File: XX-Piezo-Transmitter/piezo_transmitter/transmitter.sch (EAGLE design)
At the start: 6 parts, among them U1 BD6221FSOP, U2 ATTINY24A-SSUR

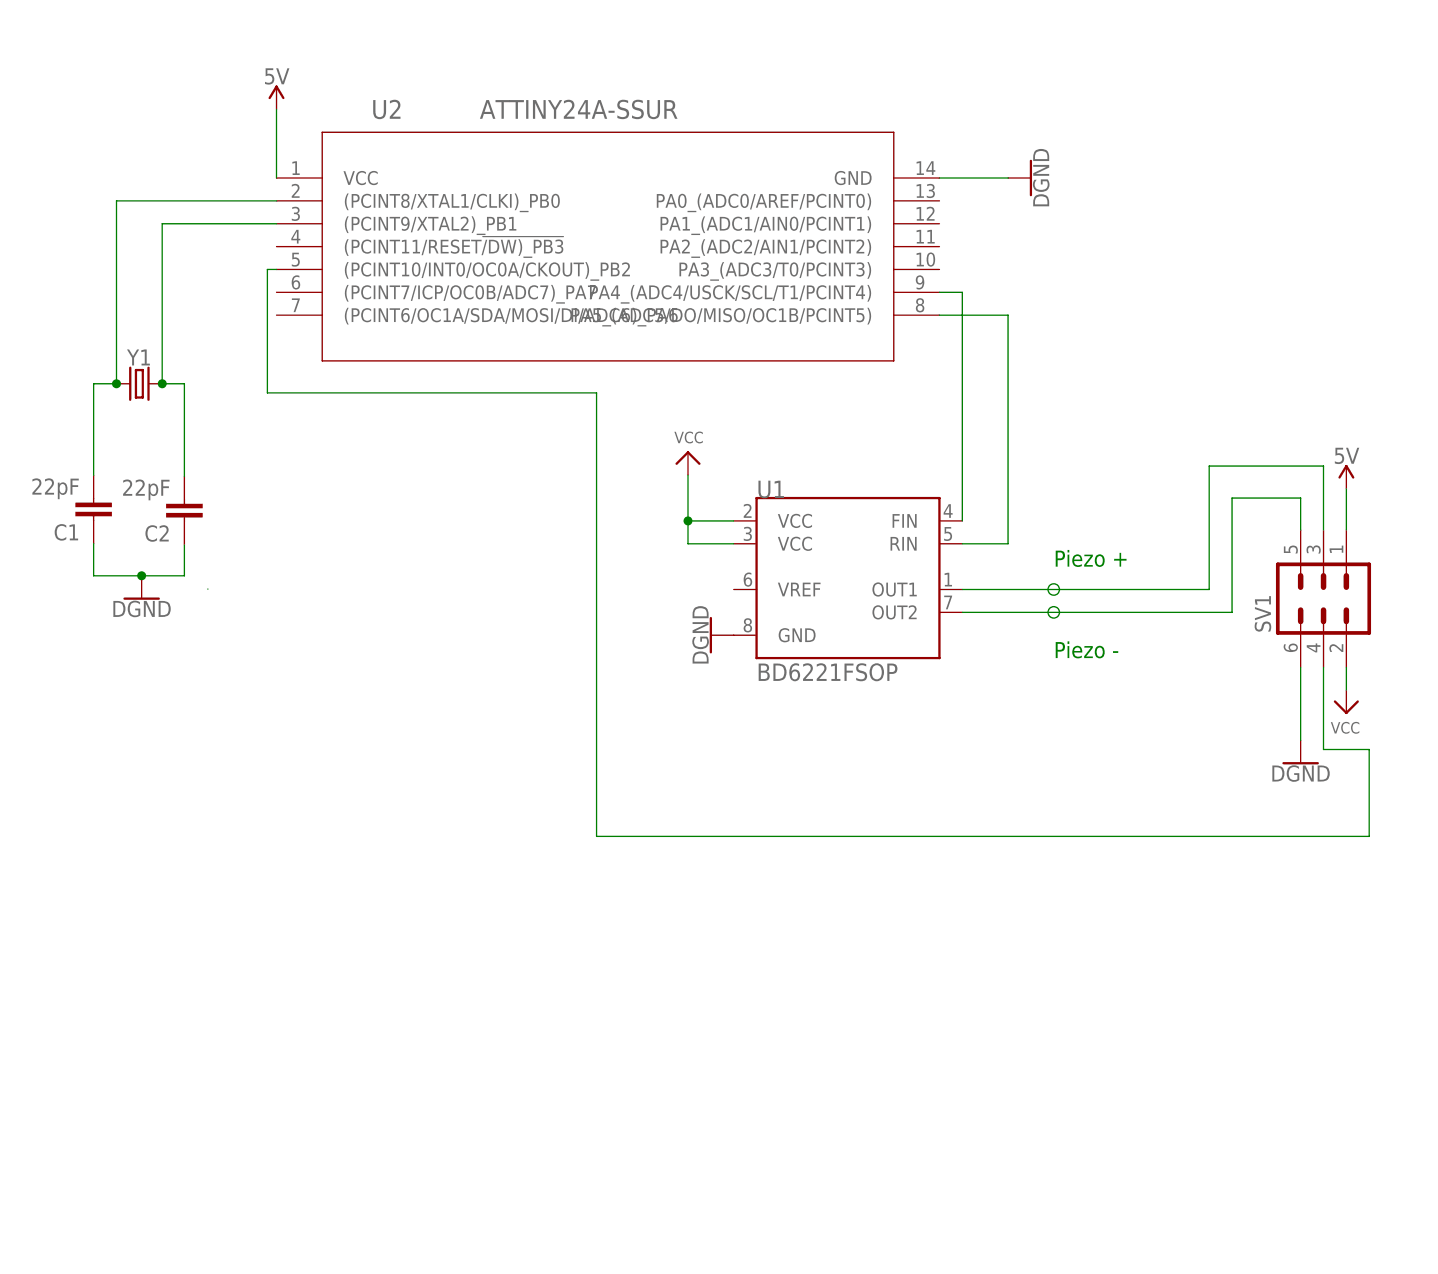
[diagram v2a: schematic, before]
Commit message: Fixed oscillator trace lengths and board trace widths. Added programmer header and mounting holes. Board about 1 squ in now.
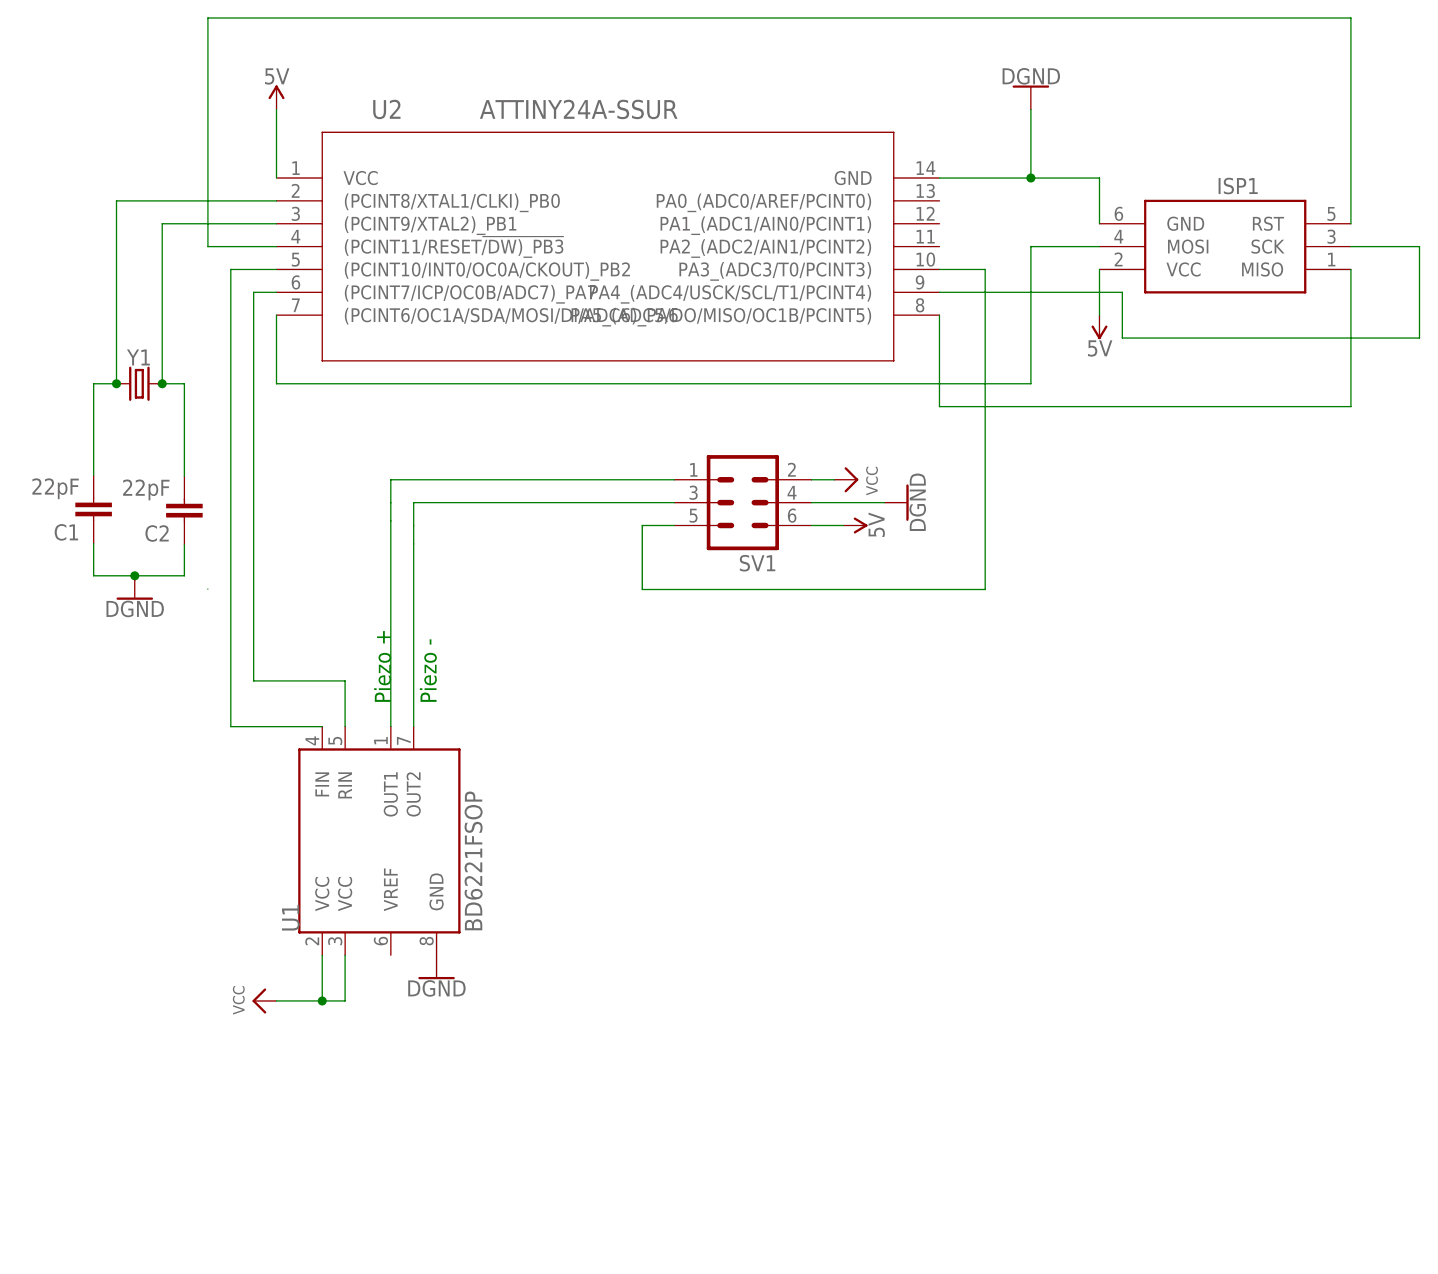
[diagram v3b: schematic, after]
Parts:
- added ISP1: AVRISP-6, adafruit:AVRISP-6
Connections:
- removed net FIN: U1.FIN, U2.PA4_(ADC4/USCK/SCL/T1/PCINT4)
- removed net PIEZO+: SV1.3, U1.OUT1
- removed net PIEZO-: SV1.5, U1.OUT2
- removed net PWM: SV1.4, U2.(PCINT10/INT0/OC0A/CKOUT)_PB2
- removed net RIN: U1.RIN, U2.PA5_(ADC5/DO/MISO/OC1B/PCINT5)
- new net N$10: U1.RIN, U2.(PCINT7/ICP/OC0B/ADC7)_PA7
- new net N$11: ISP1.SCK, U2.PA4_(ADC4/USCK/SCL/T1/PCINT4)
- new net N$12: ISP1.MISO, U2.PA5_(ADC5/DO/MISO/OC1B/PCINT5)
- new net N$4: ISP1.MOSI, U2.(PCINT6/OC1A/SDA/MOSI/DI/ADC6)_PA6
- new net N$5: SV1.5, U2.PA3_(ADC3/T0/PCINT3)
- new net N$6: ISP1.RST, U2.(PCINT11/RESET!/DW)_PB3
- new net N$7: SV1.1, U1.OUT1
- new net N$8: SV1.3, U1.OUT2
- new net N$9: U1.FIN, U2.(PCINT10/INT0/OC0A/CKOUT)_PB2
- net GND: now also ISP1.GND, SV1.4; no longer SV1.6
- net VCC_2: now also ISP1.VCC, SV1.6; no longer SV1.1
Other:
- moved on the sheet: SV1, U1

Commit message: Fixed trace names
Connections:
- net N$10 renamed RIN
- net N$11 renamed SCK
- net N$12 renamed MISO
- net N$2 renamed XTAL1
- net N$3 renamed XTAL2
- net N$4 renamed MOSI
- net N$5 renamed IO
- net N$6 renamed RESET
- net N$7 renamed PIEZO+
- net N$8 renamed PIEZO-
- net N$9 renamed FIN
- net VCC renamed 12V
- net VCC_2 renamed 5V
